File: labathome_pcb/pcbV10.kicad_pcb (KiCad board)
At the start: 2 copper layers, 100 x 100 mm, 222 parts, among them J1 PROG, J10 Fan1, J11 Fan2, J12 VPS, J13 SPK, J14 LoRa Antenna, J15 1B 2A, J16 BME280, J17 CCS811, J18 Power, J19 SPK, J2 Srvo, J20 FAN5V, J21 QWIIC, J22 AudioJack3_SwitchT, J24 AOUT, J3 I2C, J4 1wire, J5 EXT, J6 5V 3V GN 24, J7 485, J8 POWER, J9 GN 5V RGB GN, K1 G6K-2, K2 G6K-2, K3 G6K-2, Q1 BC817, Q2 BC817, Q4 BC817, Q5 IRLML6344, Q6 BC817, Q7 TIP41, Q9 IRLML6344, SW1 BTN BLUE, SW10 5V FAN 24V, SW11 PROG 5V POWER, SW12 RESET, SW2 YELLOW, SW3 GREEN, SW4 RED, SW5 BTN WHITE, SW6 OFF TERM ON, SW7 LED HTR, SW8 REL ROT, SW9 SNS MOV, U1 AMS1117, U10 LM358, U11 FUSB302BMPX, U12 BME680, U13 BME280, U14 IPS_240_240, U15 CCS811, U16 MODULE_STEPDOWN, U17 RFM95W-868S2, U18 MD8002A, U19 DS18B20, U2 ESP32-WROOM-32, U20 BH1750, U21 BTS462T, U22 AM612, U23 MPU-6050, U24 SRV05, U25 NS4168, U26 MSM261D4030H1CPM, U3 AHT21, U4 CH340C, U5 UDA1334, U6 MAX3485, U7 DS18B20, U9 RY8310, X1 FAN_6024, X2 XGZP6897D

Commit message: Minor fixes
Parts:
- moved R13 0.50 mm to (82.5, 92.2)
- moved Q6 0.40 mm to (85.8, 91.9)
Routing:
- net Net-(R21-Pad1): track 43.7 -> 42.6 mm
- net GND: track 154.7 -> 153.8 mm
- net SPI_CLK: track 47.6 -> 46.8 mm
- net K3_24: track 25.1 -> 24.4 mm
- net +3V3: track 553.5 -> 552.7 mm
- net RS485A: track 49.9 -> 49.2 mm
- net SCL: track 210.1 -> 209.5 mm

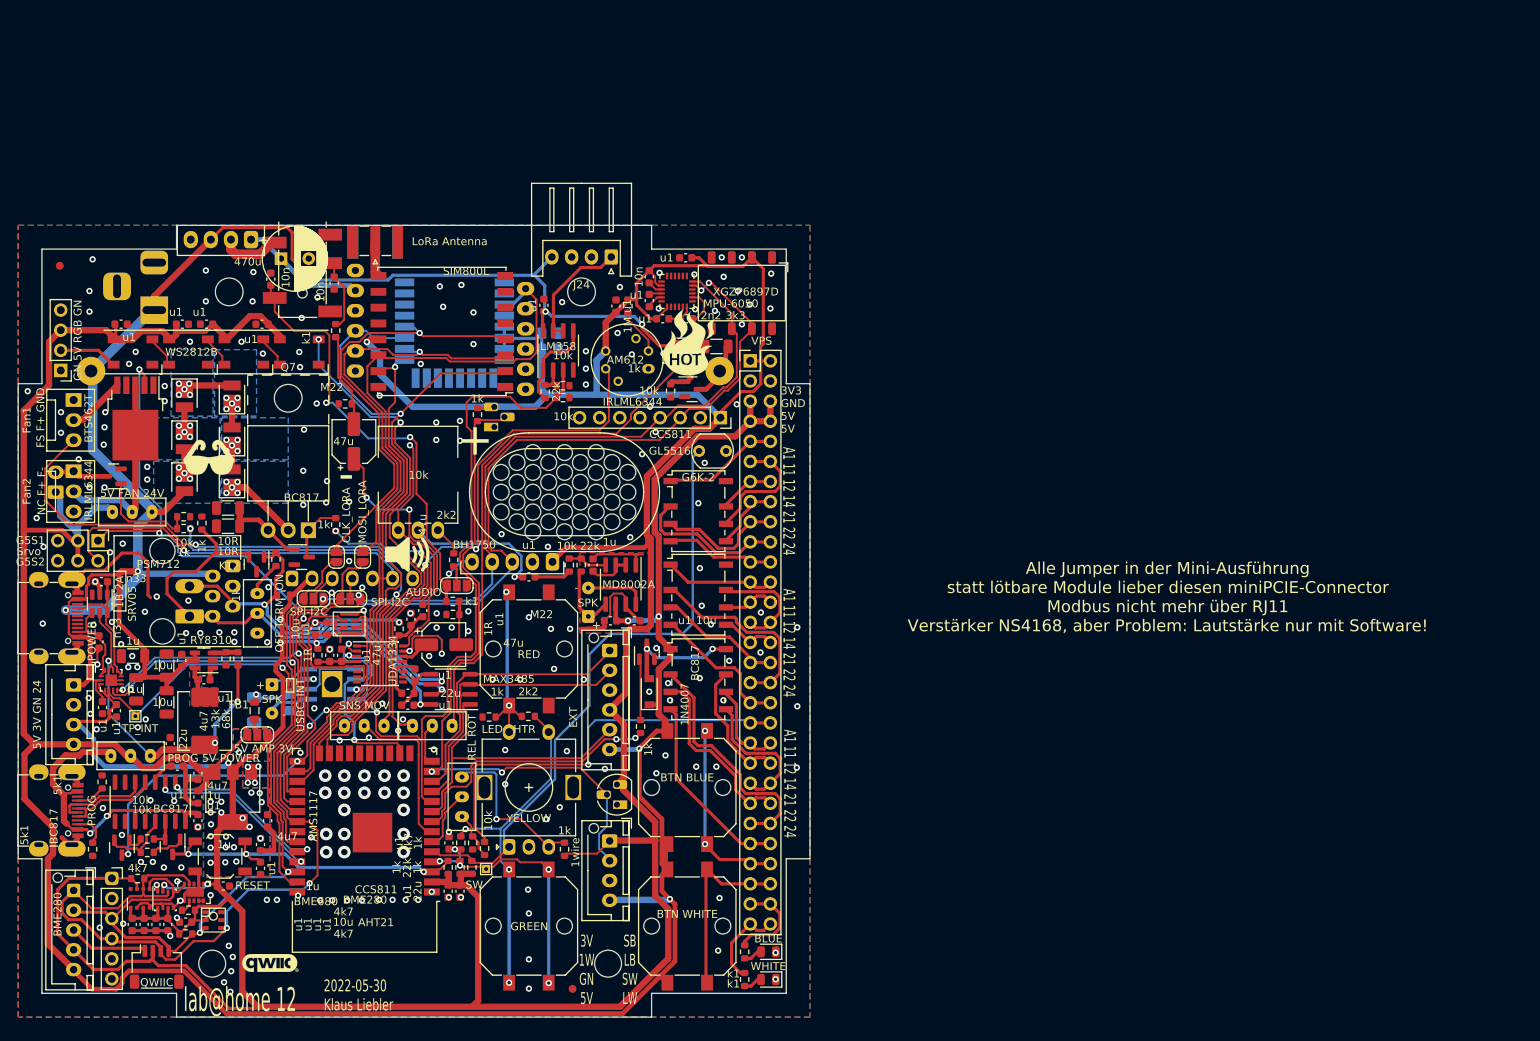
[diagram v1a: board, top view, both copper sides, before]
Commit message: Updated PCB: nRF24l01, SIM7080, LoRa module
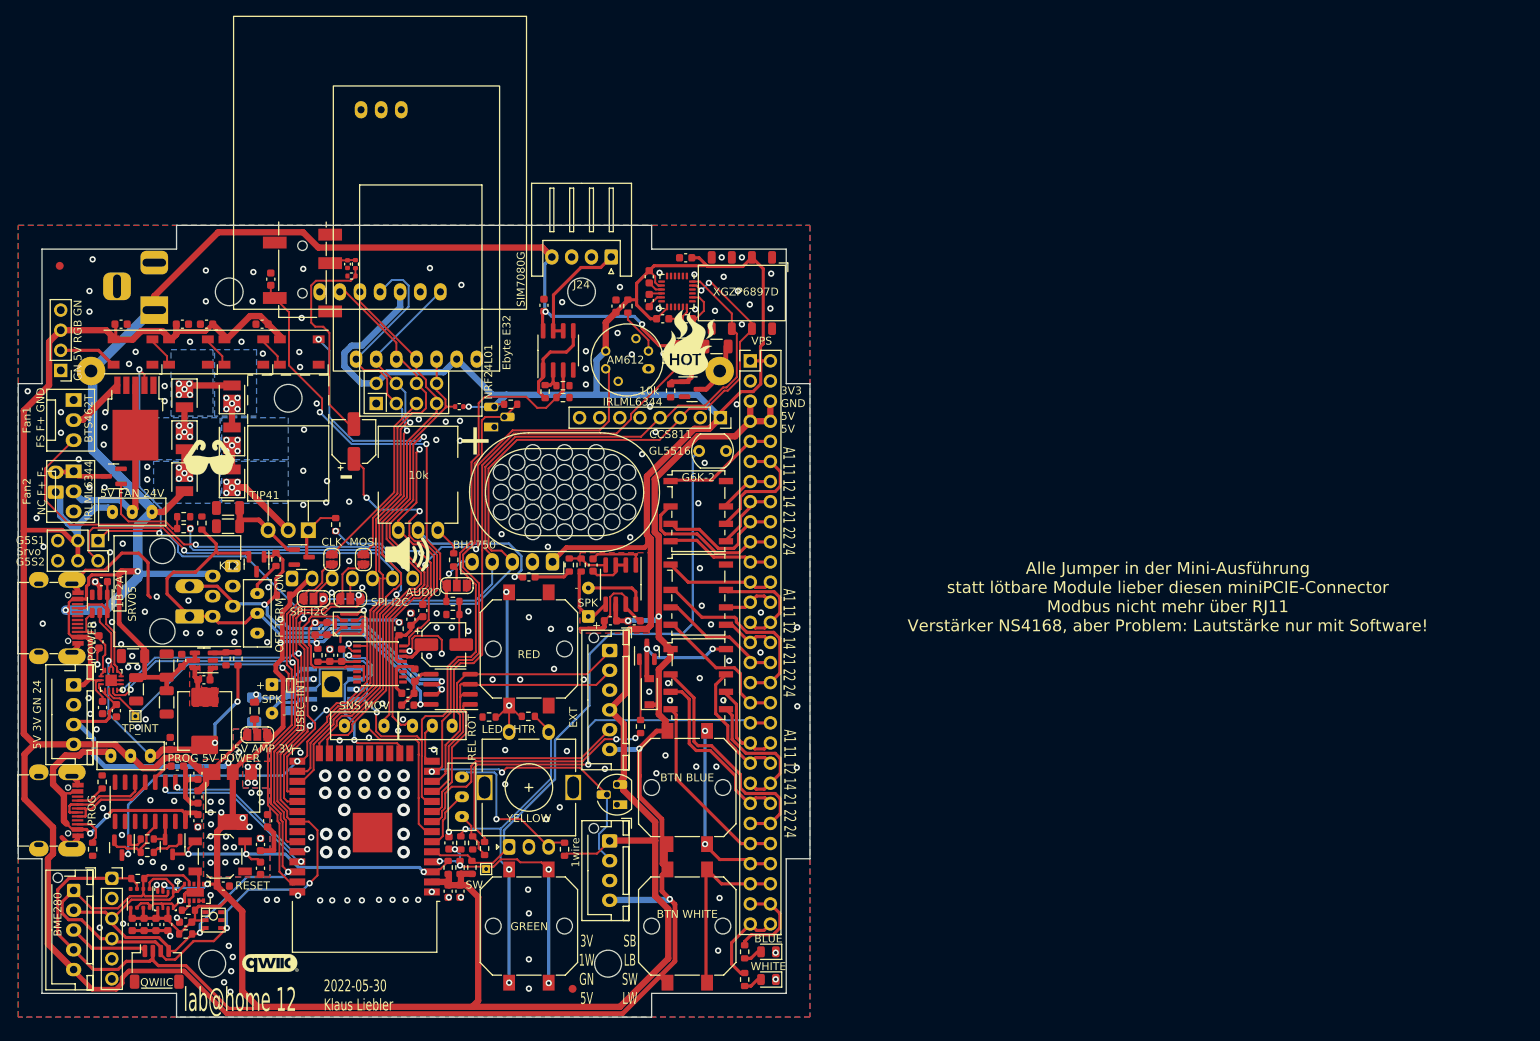
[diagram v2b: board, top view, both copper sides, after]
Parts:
- removed C27: 470u, Capacitor_THT:CP_Radial_D8.0mm_P3.50mm
- removed C40: 10u, Capacitor_SMD:C_0805_2012Metric_Pad1.18x1.45mm_HandSolder
- removed C41: u1, Capacitor_SMD:C_0805_2012Metric_Pad1.18x1.45mm_HandSolder
- removed DWM1: DWM1000, RF_Module:DWM1000
- removed GSM_Module1: SIM800L, liebler_MODULES:SIM800L
- removed J14: LoRa Antenna, Connector_Coaxial:SMA_Samtec_SMA-J-P-X-ST-EM1_EdgeMount
- removed U16: MODULE_STEPDOWN, liebler_MODULES:MODULE_STEPDOWN
- removed U17: RFM95W-868S2, RF_Module:HOPERF_RFM9XW_SMD
- added R10: 10k, Resistor_SMD:R_0402_1005Metric, F.Cu at (105.7, 72.9)
- added U8: NRF24L01, RF_Module:nRF24L01_Breakout, F.Cu at (95.2, 72.5)
- added X3: Ebyte E32, liebler_MODULES:Ebyte-E32-900T20D, F.Cu at (100.3, 66.9)
- added X4: SIM7080G, liebler_MODULES:SIM7080G_AND_MODULE, F.Cu at (95.7, 58.4)
- C49: footprint Capacitor_SMD:C_0603_1608Metric -> Capacitor_SMD:C_0402_1005Metric
- JP6: value MOSI_LORA -> MOSI
- JP7: value CLK_LORA -> CLK
- R48, R50: footprint Resistor_SMD:R_0603_1608Metric -> Resistor_SMD:R_0402_1005Metric
- moved R48 16.2 mm to (92.1, 56.4)
- moved R50 8.76 mm to (92.6, 54.9)
- moved R4 4.40 mm to (112.2, 72.6), turned to 180 degrees
- moved C49 2.94 mm to (91.6, 54.9)
- moved JP7 0.67 mm to (89.6, 92.2)
- moved JP6 0.32 mm to (93.6, 92.2)
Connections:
- JP7 pad 2: /wireless/SPI_CLKx -> SPI_CLKx
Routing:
- net /wireless/SPI_CLKx: track 55.2 -> 0.00 mm, vias 1 -> 0
- net FAN1_SENSE: track 84.1 -> 114.8 mm
- net SPI_CLKx: track 0.00 -> 22.9 mm
- net PROG_IO0: track 122.1 -> 102.8 mm, vias 2 -> 3
- net SPI_MISO: track 94.3 -> 75.7 mm, vias 1 -> 0
- net SERVO2: track 109.5 -> 127.3 mm
- net Net-(C46-Pad2): track 11.9 -> 27.8 mm
- net +4V: track 15.8 -> 0.00 mm
- net SPI_MOSIx: track 51.7 -> 42.3 mm, vias 1 -> 0
- net GND: track 153.8 -> 146.2 mm, vias 232 -> 228
- net LED_RGB: track 68.8 -> 74.0 mm
- net /analog_amp/RIGHT: track 8.47 -> 3.35 mm
- net Net-(J14-Pad1): track 4.11 -> 0.00 mm
- net +24V: track 211.9 -> 208.9 mm, vias 5 -> 4
- net +3V3: track 552.7 -> 555.4 mm
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
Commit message: PCB as ordered at JLCPCB
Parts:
- removed U21: BTS462T, Package_TO_SOT_SMD:TO-252-5_TabPin3
- added C27: 10u, Capacitor_SMD:C_1206_3216Metric, F.Cu at (66.8, 73.2)
- added C40: u1, Capacitor_SMD:C_0603_1608Metric, F.Cu at (65.2, 70.1)
- added JP8: Fan2toFan1, Jumper:SolderJumper-2_P1.3mm_Open_RoundedPad1.0x1.5mm, B.Cu at (65.5, 76.3)
- added U16: AS4950, Package_SO:SOIC-8-1EP_3.9x4.9mm_P1.27mm_EP2.29x3mm_ThermalVias, F.Cu at (62.9, 74.6)
- IMG4: value WHS -> FHOS; footprint liebler_DRAWINGS:LOGO_WHS -> liebler_DRAWINGS:LOGO_FHOS_80mm
- moved IMG4 59.9 mm to (91.7, 118.8), turned to 180 degrees
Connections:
- net Net-(J11-Pad2) renamed /VFAN
- J10 pad 1: GND -> Net-(J10-Pad1)
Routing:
- net +3V3: track 555.4 -> 590.0 mm, vias 29 -> 30
- net /VFAN: track 24.6 -> 8.42 mm
- net FAN2_DRIVE: track 58.0 -> 72.3 mm
- net FAN1_DRIVE: track 82.7 -> 71.6 mm
- net +24V: track 208.9 -> 218.7 mm
- net Net-(J10-Pad1): track 0.00 -> 8.27 mm
- net GND: track 146.2 -> 149.8 mm, vias 228 -> 221
- net Net-(J10-Pad2): track 7.30 -> 5.30 mm
- net Net-(JP8-Pad2): track 0.00 -> 1.39 mm, vias 0 -> 1
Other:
- board text added: "2022-09-28 Klaus Liebler"
- board text added: "lab@home 13"
- board text removed: "2022-05-30 Klaus Liebler"
- board text removed: "lab@home 12"
